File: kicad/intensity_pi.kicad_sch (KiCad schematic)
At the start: 67 parts, among them J1 Input A, J2 Input B / Setpoint, J3 Monitor, J4 Output, J7 select 1, SW1 SW_SPDT, SW2 SW_SPDT, SW3 SW_SPDT, SW5 EG6100-ND, U1 LM4040DBZ-5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

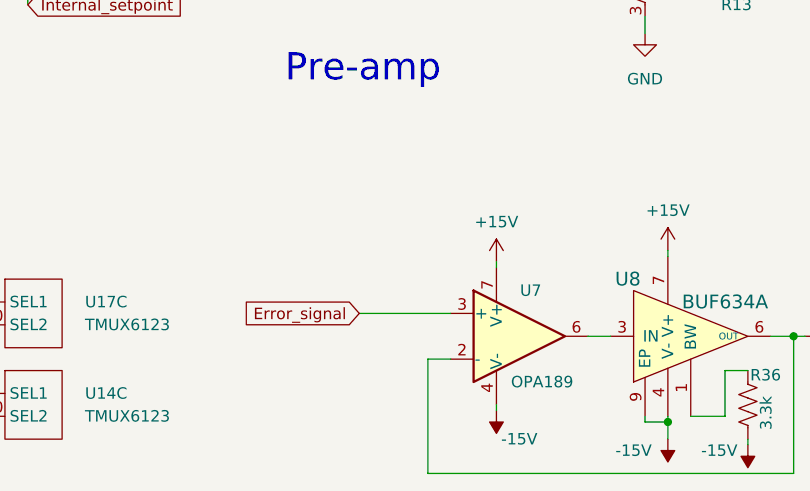
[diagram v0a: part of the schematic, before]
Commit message: different way to route design
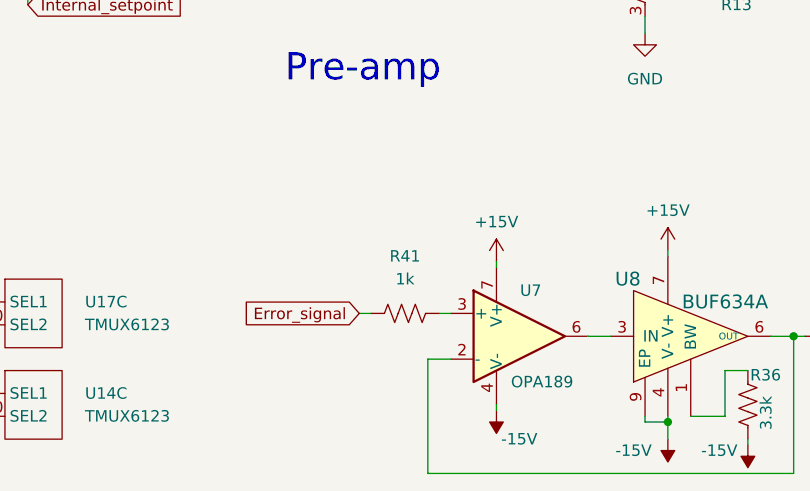
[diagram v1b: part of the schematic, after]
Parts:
- added R41: 1k, Resistor_SMD:R_0805_2012Metric, symbol Device:R_US
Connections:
- net Error_signal: now also R41.2; no longer U7.3 (+)
- new net: R41.1, U7.3 (+)
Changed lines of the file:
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@@
 	(wire
 		(pts
+			(xy 109.22 179.07) (xy 110.49 179.07)
+		)
+		(stroke
+			(width 0)
+			(type default)
+		)
+	)
+	(wire
+		(pts
 			(xy 165.1 64.77) (xy 165.1 58.42)
 		)
@@
 	(wire
 		(pts
-			(xy 109.22 179.07) (xy 119.38 179.07)
-		)
-		(stroke
-			(width 0)
-			(type default)
-		)
-	)
-	(wire
-		(pts
 			(xy 219.71 114.3) (xy 234.315 114.3)
 		)
@@
 	(wire
 		(pts
+			(xy 118.11 179.07) (xy 119.38 179.07)
+		)
+		(stroke
+			(width 0)
+			(type default)
+		)
+	)
+	(wire
+		(pts
 			(xy 138.43 30.48) (xy 140.97 30.48)
 		)
@@
 					(unit 1)
 				)
+			)
+		)
+	)
+	(symbol
+		(lib_id "Device:R_US")
+		(at 114.3 179.07 270)
+		(unit 1)
+		(exclude_from_sim no)
+		(in_bom yes)
+		(on_board yes)
+		(dnp no)
+		(fields_autoplaced yes)
+		(property "Reference" "R41"
+			(at 114.3 172.72 90)
+			(effects
+				(font
+					(size 1.27 1.27)
+				)
+			)
+		)
+		(property "Value" "1k"
+			(at 114.3 175.26 90)
+			(effects
+				(font
+					(size 1.27 1.27)
+				)
+			)
+		)
+		(property "Footprint" "Resistor_SMD:R_0805_2012Metric"
+			(at 114.046 180.086 90)
+			(effects
+				(font
+					(size 1.27 1.27)
+				)
+				(hide yes)
+			)
+		)
+		(property "Datasheet" "~"
+			(at 114.3 179.07 0)
+			(effects
+				(font
+					(size 1.27 1.27)
+				)
+				(hide yes)
+			)
+		)
+		(property "Description" ""
+			(at 114.3 179.07 0)
+			(effects
+				(font
+					(size 1.27 1.27)
+				)
+				(hide yes)
+			)
+		)
+		(property "DIGIKEY" ""
+			(at 114.3 179.07 0)
+			(effects
+				(font
+					(size 1.27 1.27)
+				)
+				(hide yes)
+			)
+		)
+		(property "MPN" ""
+			(at 114.3 179.07 0)
+			(effects
+				(font
+					(size 1.27 1.27)
+				)
+				(hide yes)
+			)
+		)
+		(pin "1"
+		)
+		(pin "2"
+		)
+		(instances
+			(project "intensity_pi"
+				(path "/3a3d7bcb-6fa5-41ef-9ea1-6d4ab7c492fd"
+					(reference "R41")
+					(unit 1)
+				)
